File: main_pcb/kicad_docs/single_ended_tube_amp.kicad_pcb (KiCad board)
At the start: 2 copper layers, 190.5 x 115.6 mm, 54 parts, among them J1 in_pcb, J2 ts_pcb, J3 gain_pcb, J4 pa_pcb, J5 ac_htr_pcb, J6 pa_b+_pcb, J7 high_voltage_pcb, J8 dc_htr_pcb

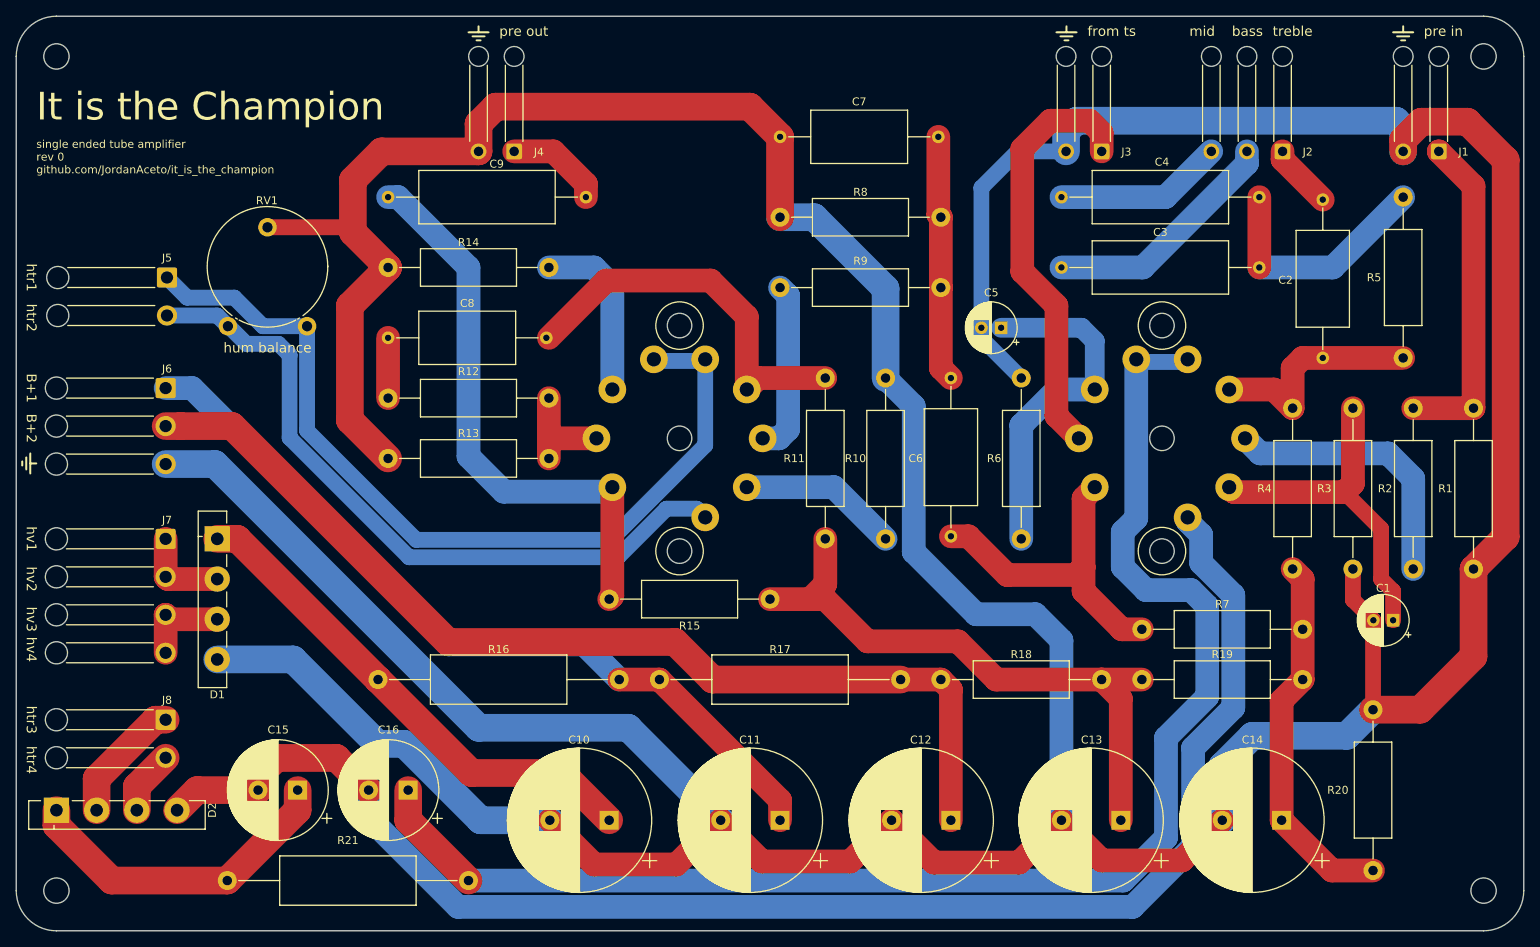
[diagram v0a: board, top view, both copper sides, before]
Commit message: tweak DC heater, pcb, regenerate build files
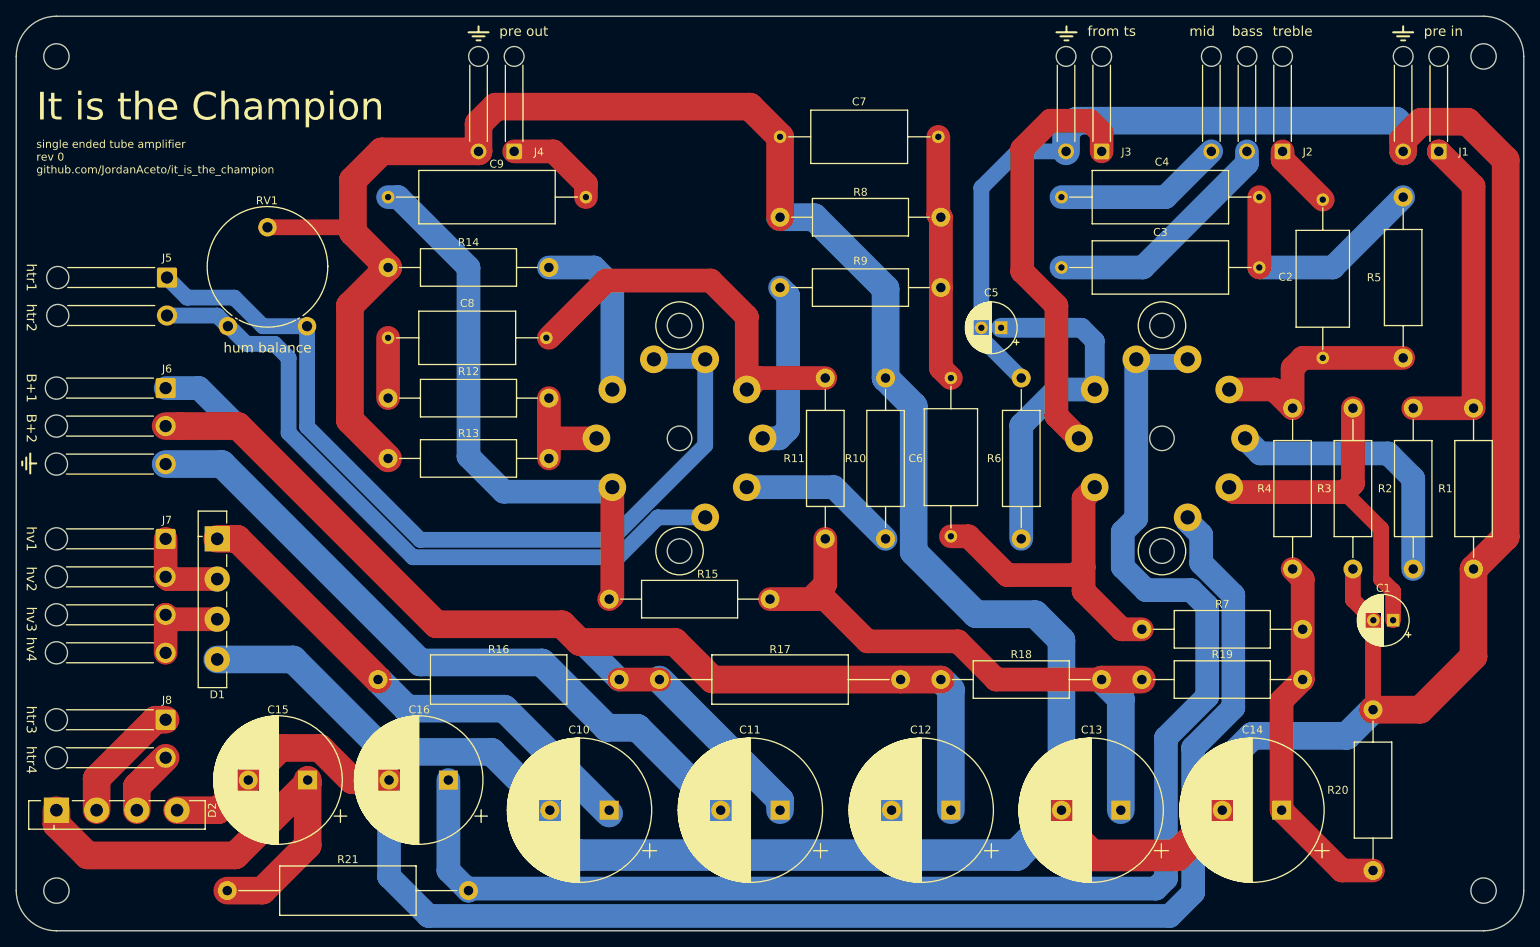
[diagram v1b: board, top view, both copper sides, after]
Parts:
- C15, C16: value 4700u 10v -> 10000u 10v; footprint Capacitor_THT:CP_Radial_D12.5mm_P5.00mm -> Capacitor_THT:CP_Radial_D16.0mm_P7.50mm
- R21: value ? -> 3R3 5W
- moved C16 5.24 mm to (44.5, 121.9)
- moved C15 1.80 mm to (26.7, 121.9)
- moved C10 1.27 mm to (64.8, 125.7)
- moved C11 1.27 mm to (86.4, 125.7)
- moved C12 1.27 mm to (108.0, 125.7)
- moved C13 1.27 mm to (129.4, 125.7)
- moved C14 1.27 mm to (149.7, 125.7)
- moved R21 1.27 mm to (47.0, 135.9)
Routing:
- net Net-(C15-Pad1): track 41.5 -> 60.1 mm
- net Earth: track 891.2 -> 906.0 mm
- net Net-(C16-Pad1): track 182.8 -> 186.8 mm
- net Net-(J5-Pad2): track 89.8 -> 88.3 mm
- net B+_3: track 78.4 -> 77.1 mm
- net B+_1: track 101.7 -> 100.5 mm
- net B+_2: track 129.5 -> 128.3 mm
- net B+_4: track 47.6 -> 46.8 mm
